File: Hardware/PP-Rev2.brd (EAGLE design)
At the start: 190.5 x 101.3 mm, 181 parts, among them IC1 LT6004, IC2 TLC6C5912-Q1, J1 J_0399700102, Q1 MOSFET-PCHANNEL, Q10 2N7002PW, Q11 2N7002PW, Q12 2N7002PW, Q13 2N7002PW, Q14 2N7002PW, Q15 2N7002PW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

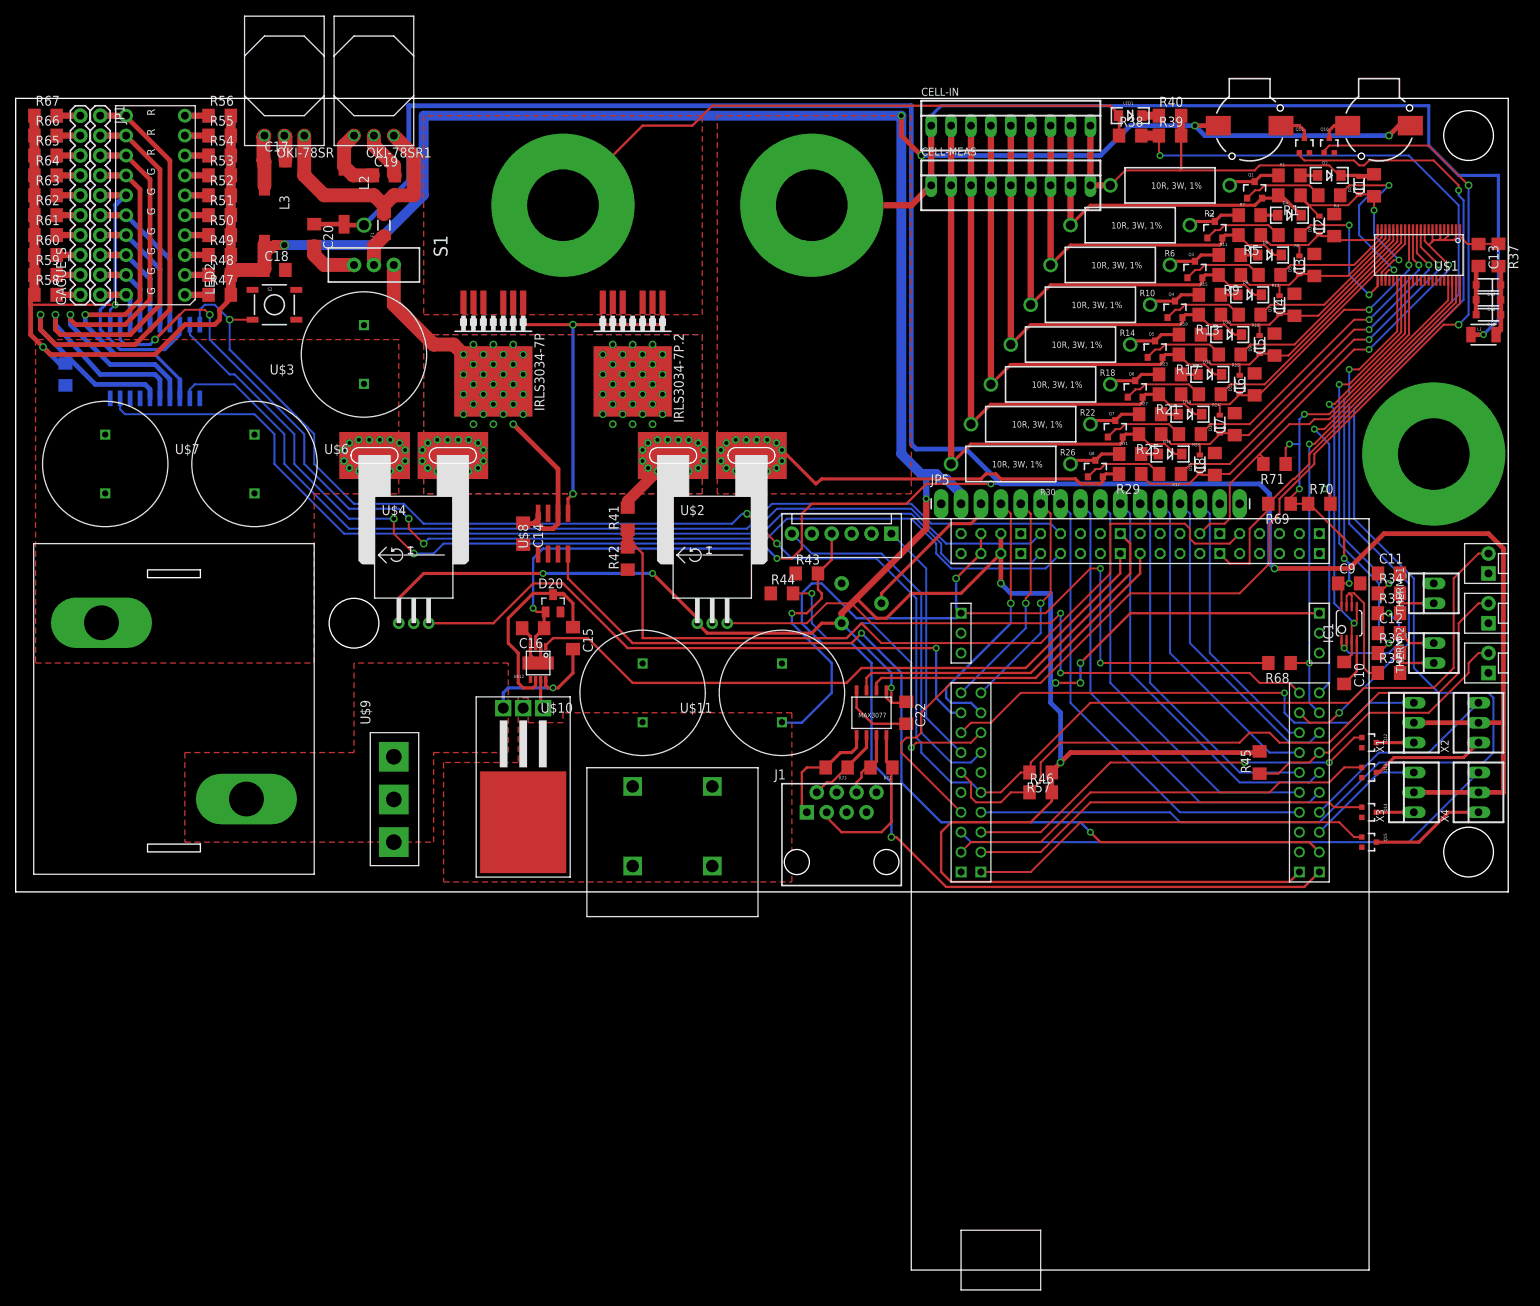
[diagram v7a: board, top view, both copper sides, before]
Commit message: Fixed lots of DRC errors. Just a few overlaps left.
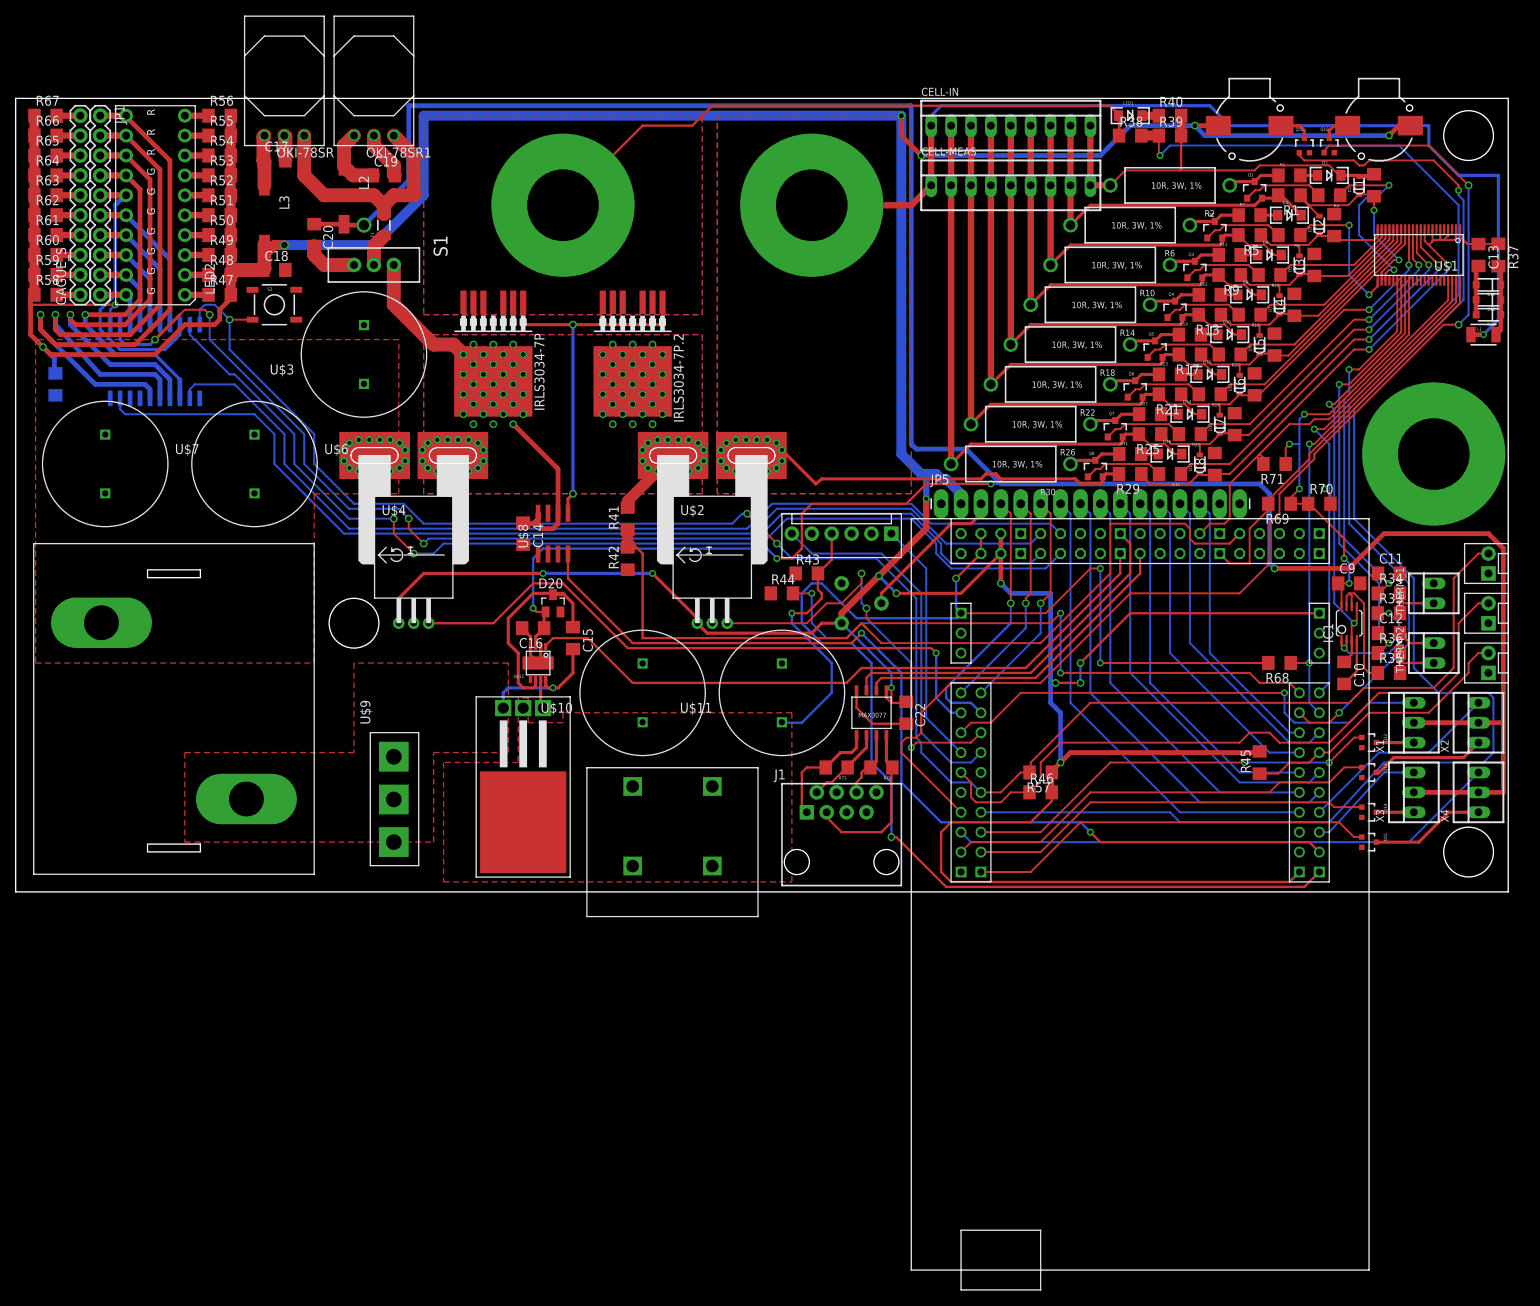
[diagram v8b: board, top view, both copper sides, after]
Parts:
- moved C21 1.80 mm to (5.08, 64.8)
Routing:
- net PACK_I_MEAS: track 84.3 -> 91.2 mm, vias 2 -> 4
- net 5V: track 633.7 -> 629.7 mm, vias 16 -> 18
- net CELL_8: track 174.2 -> 172.7 mm
- net V_CHECK_OUT: track 129.1 -> 130.1 mm
- added copper zone on layer 16, net CELL_8
- added copper zone on layer 16, net N$37
